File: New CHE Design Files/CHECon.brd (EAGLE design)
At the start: 81.7 x 51.7 mm, 42 parts, among them U2 MAX232SOIC16, U3 RS485SOIC

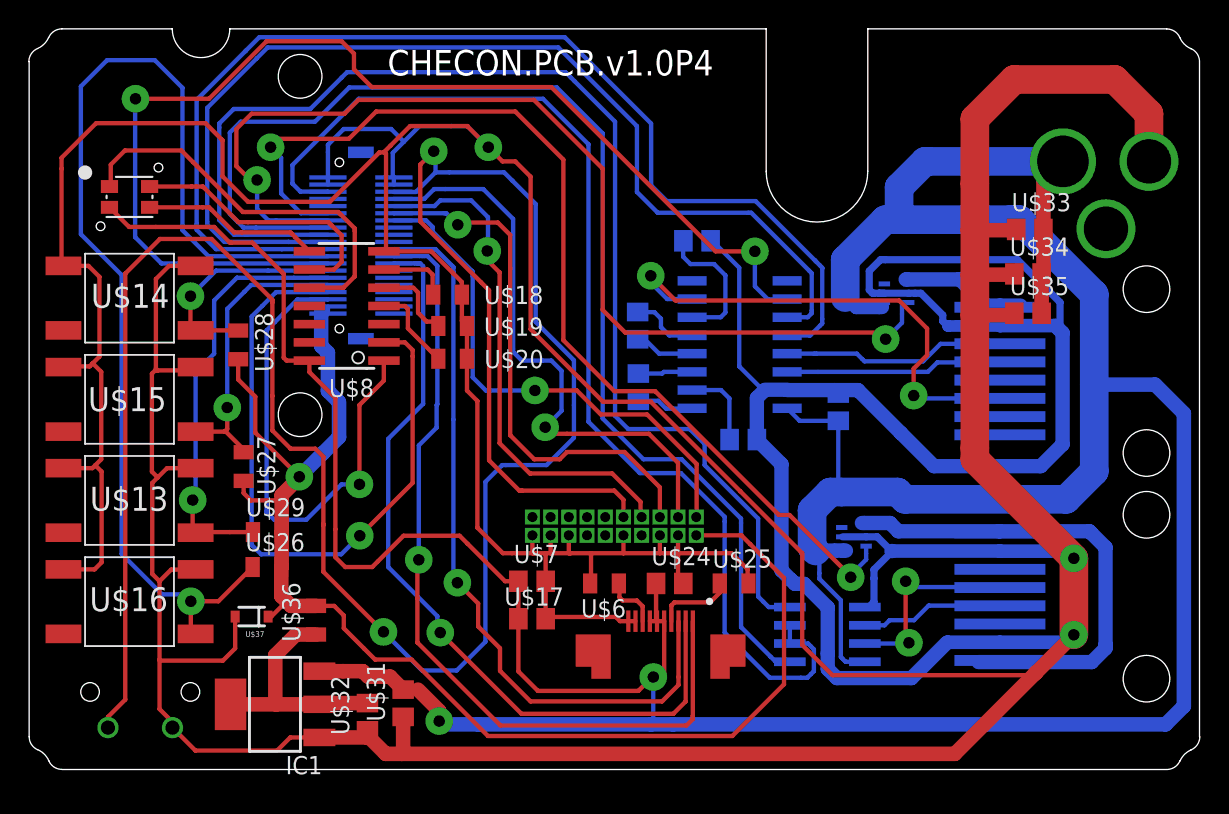
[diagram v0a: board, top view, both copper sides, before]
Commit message: P4
Fixed MAX232 rail, moved to 3.3V
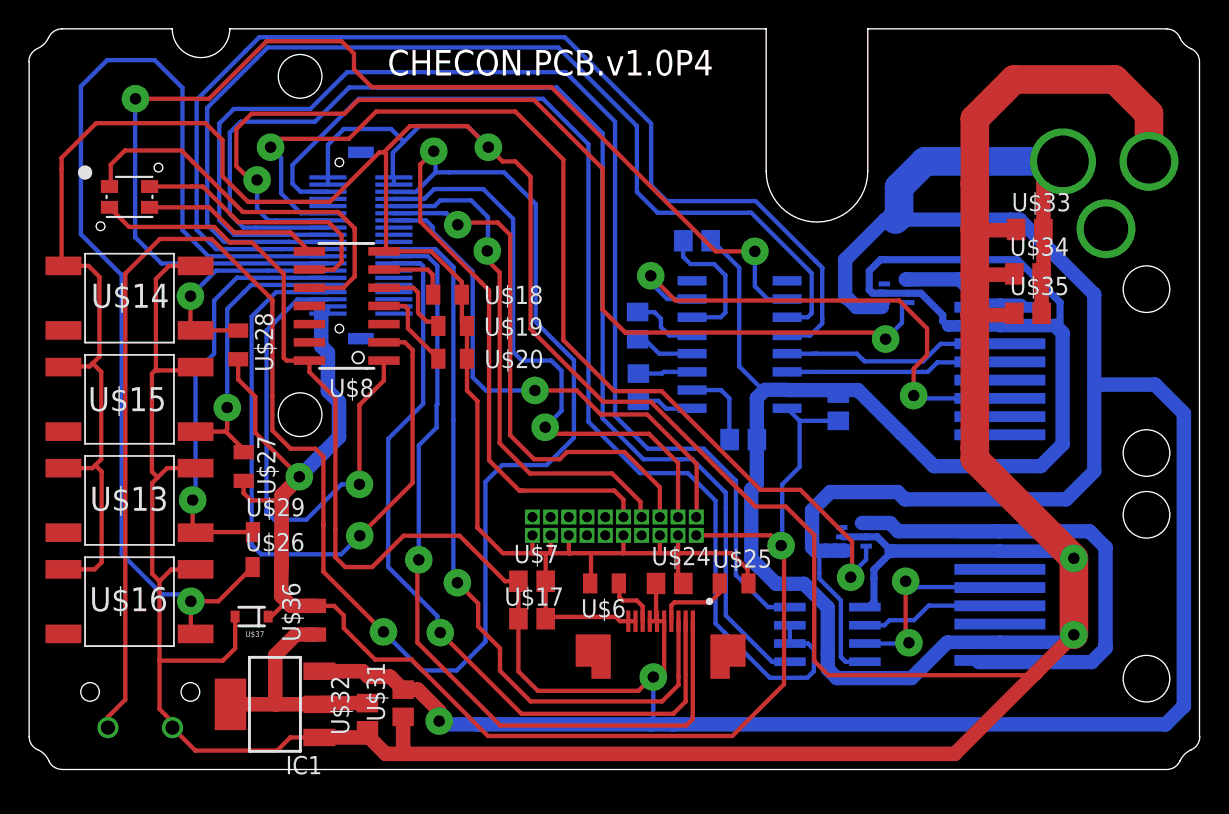
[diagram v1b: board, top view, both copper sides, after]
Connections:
- net +3V3: now also U$21.1, U2.16
- net V+: no longer U$21.1, U2.16
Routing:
- net +3V3: track 93.9 -> 108.2 mm, vias 1 -> 2
- net V+: track 281.2 -> 273.3 mm
- net GND: track 562.2 -> 565.1 mm
- net N$39: track 72.4 -> 73.9 mm
- net N$17: track 86.0 -> 86.5 mm

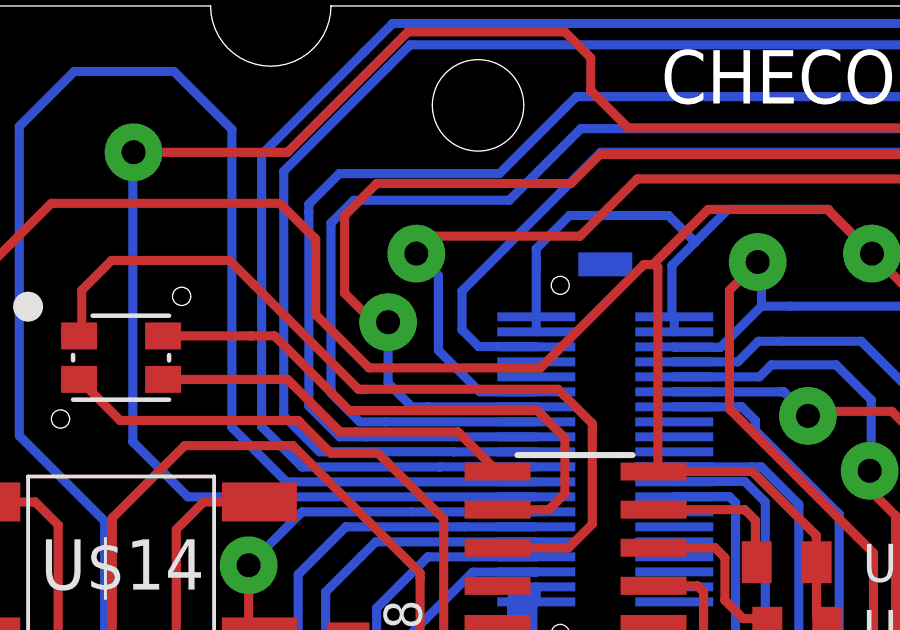
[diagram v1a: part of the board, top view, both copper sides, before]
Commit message: P4 update
Moved scanner power select to PTD3 to avoid conflict with EEPROM CS
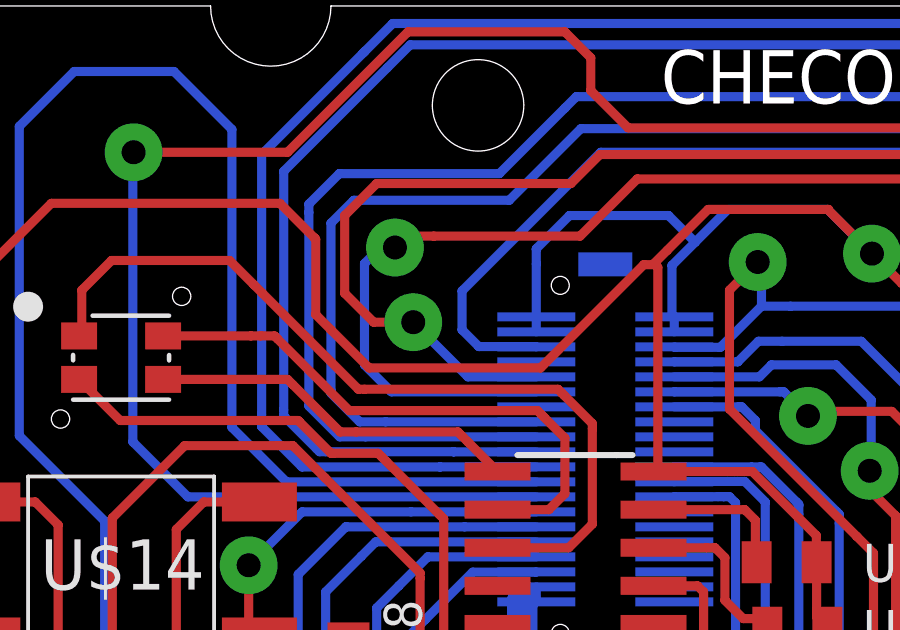
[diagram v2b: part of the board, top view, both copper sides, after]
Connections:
- net N$40: now also U$10.P$9; no longer U$10.P$13
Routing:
- net N$39: track 73.9 -> 77.9 mm
- net N$40: track 74.0 -> 72.4 mm
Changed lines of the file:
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@@
 <wire x1="12.9261" y1="-4.7269" x2="11.7094" y2="-5.9436" width="0.3048" layer="16"/>
 <via x="11.6332" y="-10.2108" extent="1-16" drill="0.8" diameter="1.9304"/>
-<wire x1="-20.3454" y1="6.096" x2="-19.9784" y2="5.9688" width="0" layer="19" extent="16-16"/>
 <wire x1="11.7094" y1="-5.9436" x2="11.7094" y2="-10.1346" width="0.3048" layer="16"/>
 <wire x1="11.7094" y1="-10.1346" x2="11.6332" y2="-10.2108" width="0.3048" layer="16"/>
@@
 <wire x1="11.8364" y1="-19.8882" x2="11.8364" y2="-10.414" width="0.3048" layer="1"/>
 <wire x1="11.8364" y1="-10.414" x2="11.6332" y2="-10.2108" width="0.3048" layer="1"/>
+<wire x1="-20.3454" y1="6.096" x2="-19.9784" y2="5.9688" width="0" layer="19" extent="16-16"/>
 </signal>
 <signal name="N$13">
@@
 <contactref element="U$5" pad="3"/>
 <contactref element="U$10" pad="P$11"/>
-<wire x1="-19.9784" y1="12.9688" x2="-21.8588" y2="12.9688" width="0.3048" layer="16"/>
-<wire x1="-21.8588" y1="12.9688" x2="-23.241" y2="14.351" width="0.3048" layer="16"/>
-<via x="-23.9776" y="17.5768" extent="1-16" drill="0.8" diameter="1.9304"/>
+<via x="-24.6888" y="17.78" extent="1-16" drill="0.8" diameter="1.9304"/>
 <wire x1="-6.9088" y1="20.066" x2="-3.556" y2="16.7132" width="0.3048" layer="1"/>
 <wire x1="-3.556" y1="16.7132" x2="-3.556" y2="4.1148" width="0.3048" layer="1"/>
@@
 <wire x1="17.5632" y1="-10.2512" x2="17.5632" y2="-10.7578" width="0.3048" layer="16"/>
 <wire x1="17.5632" y1="-10.7578" x2="17.5632" y2="-11.1642" width="0.3048" layer="16"/>
-<wire x1="-23.241" y1="14.351" x2="-23.241" y2="16.8402" width="0.3048" layer="16"/>
-<wire x1="-23.241" y1="16.8402" x2="-23.9776" y2="17.5768" width="0.3048" layer="16"/>
 <wire x1="-18.5166" y1="18.161" x2="-23.3934" y2="18.161" width="0.3048" layer="1"/>
-<wire x1="-23.3934" y1="18.161" x2="-23.9776" y2="17.5768" width="0.3048" layer="1"/>
 <wire x1="17.5632" y1="-11.1642" x2="17.5632" y2="-11.1896" width="0.3048" layer="16"/>
 <wire x1="17.5632" y1="-11.1896" x2="16.4465" y2="-12.3063" width="0.3048" layer="16"/>
@@
 <wire x1="16.5862" y1="-9.9314" x2="16.5862" y2="-12.319" width="0.3048" layer="1"/>
 <wire x1="16.5862" y1="-12.319" x2="16.4846" y2="-12.4206" width="0.3048" layer="1"/>
+<wire x1="-23.3934" y1="18.161" x2="-24.3078" y2="18.161" width="0.3048" layer="1"/>
+<wire x1="-24.3078" y1="18.161" x2="-24.6888" y2="17.78" width="0.3048" layer="1"/>
+<wire x1="-24.6888" y1="17.78" x2="-25.1714" y2="17.78" width="0.3048" layer="16"/>
+<wire x1="-25.1714" y1="17.78" x2="-25.7048" y2="17.2466" width="0.3048" layer="16"/>
+<wire x1="-25.7048" y1="17.2466" x2="-25.7048" y2="13.8684" width="0.3048" layer="16"/>
+<wire x1="-25.7048" y1="13.8684" x2="-24.8412" y2="13.0048" width="0.3048" layer="16"/>
+<wire x1="-19.9784" y1="12.9688" x2="-24.8052" y2="12.9688" width="0.3048" layer="16"/>
+<wire x1="-24.8052" y1="12.9688" x2="-24.8412" y2="13.0048" width="0.3048" layer="16"/>
 </signal>
 <signal name="N$40">
 <contactref element="U$4" pad="3"/>
-<contactref element="U$10" pad="P$13"/>
-<wire x1="-19.9784" y1="12.4688" x2="-23.594" y2="12.4688" width="0.3048" layer="16"/>
-<via x="-24.9174" y="15.2908" extent="1-16" drill="0.8" diameter="1.9304"/>
+<via x="-24.0792" y="15.2908" extent="1-16" drill="0.8" diameter="1.9304"/>
 <wire x1="-26.3652" y1="18.8468" x2="-25.2984" y2="19.9136" width="0.3048" layer="1"/>
 <wire x1="-25.2984" y1="19.9136" x2="-18.8214" y2="19.9136" width="0.3048" layer="1"/>
@@
 <wire x1="18.4658" y1="4.6482" x2="18.923" y2="4.191" width="0.3048" layer="1"/>
 <wire x1="-26.3652" y1="18.8468" x2="-26.3652" y2="16.256" width="0.3048" layer="1"/>
-<wire x1="-23.594" y1="12.4688" x2="-24.1274" y2="12.4688" width="0.3048" layer="16"/>
 <wire x1="20.535" y1="6.7414" x2="20.0778" y2="6.7414" width="0.3048" layer="16"/>
 <wire x1="20.0778" y1="6.7414" x2="20.066" y2="6.7296" width="0.3048" layer="16"/>
 <wire x1="-26.3652" y1="16.256" x2="-25.4" y2="15.2908" width="0.3048" layer="1"/>
-<wire x1="-25.4" y1="15.2908" x2="-24.9174" y2="15.2908" width="0.3048" layer="1"/>
-<wire x1="-24.1274" y1="12.4688" x2="-24.9174" y2="13.2588" width="0.3048" layer="16"/>
-<wire x1="-24.9174" y1="13.2588" x2="-24.9174" y2="15.2908" width="0.3048" layer="16"/>
+<contactref element="U$10" pad="P$9"/>
+<wire x1="-25.4" y1="15.2908" x2="-24.0792" y2="15.2908" width="0.3048" layer="1"/>
+<wire x1="-19.9784" y1="13.4688" x2="-22.2572" y2="13.4688" width="0.3048" layer="16"/>
+<wire x1="-22.2572" y1="13.4688" x2="-24.0792" y2="15.2908" width="0.3048" layer="16"/>
 </signal>
 <signal name="N$5">
